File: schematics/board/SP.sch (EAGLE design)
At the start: 33 parts

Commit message: Плата СБ
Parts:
- added S1: (no value), CanCubeSat:255SB
- added U$1, U$2, U$20, U$21: KCONNECT--, CanCubeSat:KCONNECT--
- added U$18, U$3, U$4: KCONNECT4, CanCubeSat:KCONNECT4
- added U$19: KCONNECT1, CanCubeSat:KCONNECT1
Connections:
- removed net N$17: D24.C
- removed net N$18: D25.A
- removed net N$20: D26.A
- removed net N$23: D27.C
- removed net N$24: D28.A
- removed net N$26: D29.A
- removed net N$27: D29.C
- removed net N$29: SOL1.IN
- removed net N$30: D1.C, SOL16.OUT
- removed net N$31: D31.C
- removed net N$32: D32.A
- removed net N$33: D32.C
- removed net N$34: D33.A
- removed net N$35: D33.C
- removed net N$36: D34.A
- removed net N$37: D34.C
- removed net N$38: D35.A
- removed net N$39: D35.C
- removed net N$40: D36.A
- removed net N$41: D36.C
- removed net N$42: D37.A
- removed net N$43: D37.C
- removed net N$44: D38.A
- removed net N$45: D1.A, D38.C
- new net BUS+1: D1.A, D1.C, D38.C, U$1.P$1, U$18.P$1, U$20.P$1, U$3.P$1
- new net BUS-1: D29.A, S1.S, SOL1.IN
- new net N$2: S1.P, U$19.P$1, U$2.P$1, U$21.P$1, U$4.P$1
- net N$1: now also D29.C; no longer SOL1.OUT
- net N$10: now also D32.C, D33.A; no longer SOL10.OUT
- net N$11: now also D33.C, D34.A; no longer SOL11.OUT
- net N$12: now also D34.C, D35.A; no longer SOL12.OUT
- net N$13: now also D35.C, D36.A; no longer SOL13.OUT
- net N$14: now also D36.C, D37.A; no longer SOL14.OUT
- net N$15: now also D37.C, D38.A; no longer SOL15.OUT
- net N$16: no longer SOL2.OUT
- net N$19: now also D26.A; no longer SOL4.OUT
- net N$22: no longer SOL5.OUT
- net N$28: no longer SOL7.OUT
- net N$3: now also D24.C, D25.A; no longer SOL3.OUT
- net N$6: now also D27.C, D28.A; no longer SOL6.OUT
- net N$8: no longer SOL8.OUT
- net N$9: now also D31.C, D32.A; no longer SOL9.OUT

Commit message: Плата СБ
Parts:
- added LED1: LAP4-BOTTOM, led:LAP4-BOTTOM
- added R1: 2k7, rcl:R-US_R0603
- SOL1, SOL10, SOL11, SOL13, SOL14, SOL15, SOL2, SOL3, SOL5, SOL6, SOL7, SOL9: value SOLAR -> SOLAR_0; device CanCubeSat:SOLAR -> CanCubeSat:SOLAR_0
- SOL12, SOL16, SOL4, SOL8: value SOLARSOLAR_1 -> SOLAR_1; device CanCubeSat:SOLARSOLAR_1 -> CanCubeSat:SOLAR_1
- U$1, U$2, U$20, U$21: value KCONNECT-- -> KCONNECT3; device CanCubeSat:KCONNECT-- -> CanCubeSat:KCONNECT3
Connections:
- new net N$4: D1.A, D38.C, SOL16.OUT
- new net N$5: LED1.A, R1.1
- net BUS+1: now also R1.2; no longer D1.A, D38.C
- net N$1: now also SOL1.OUT
- net N$10: now also SOL10.OUT
- net N$11: now also SOL11.OUT
- net N$12: now also SOL12.OUT
- net N$13: now also SOL13.OUT
- net N$14: now also SOL14.OUT
- net N$15: now also SOL15.OUT
- net N$16: now also SOL2.OUT
- net N$19: now also SOL4.OUT
- net N$2: now also LED1.C
- net N$22: now also SOL5.OUT
- net N$28: now also SOL7.OUT
- net N$3: now also SOL3.OUT
- net N$6: now also SOL6.OUT
- net N$8: now also SOL8.OUT
- net N$9: now also SOL9.OUT

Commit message: Плата SP
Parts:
- removed LED1: LAP4-BOTTOM, led:LAP4-BOTTOM
- added PWR: (no value), led:LEDCHIPLED_0603
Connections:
- new net N$7: PWR.C
- net N$2: no longer LED1.C
- net N$5: now also PWR.A; no longer LED1.A
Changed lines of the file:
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@@
 <part name="U$21" library="CanCubeSat" deviceset="KCONNECT" device="3" value="KCONNECT3"/>
 <part name="S1" library="CanCubeSat" deviceset="255SB" device="" package3d_urn="urn:adsk.eagle:package:27679/1"/>
-<part name="LED1" library="led" library_urn="urn:adsk.eagle:library:259" deviceset="*P4" device="-BOTTOM" package3d_urn="urn:adsk.eagle:package:15878/1" technology="LA"/>
 <part name="R1" library="rcl" library_urn="urn:adsk.eagle:library:334" deviceset="R-US_" device="R0603" package3d_urn="urn:adsk.eagle:package:23555/3" value="2k7"/>
+<part name="PWR" library="led" library_urn="urn:adsk.eagle:library:259" deviceset="LED" device="CHIPLED_0603" package3d_urn="urn:adsk.eagle:package:15822/2"/>
 </parts>
 <sheets>
@@
 <attribute name="VALUE" x="36.83" y="-20.955" size="1.778" layer="96" rot="R270"/>
 </instance>
-<instance part="LED1" gate="G$1" x="66.04" y="7.62" smashed="yes">
-<attribute name="NAME" x="69.596" y="3.048" size="1.778" layer="95" rot="R90"/>
-<attribute name="VALUE" x="71.755" y="3.048" size="1.778" layer="96" rot="R90"/>
-</instance>
 <instance part="R1" gate="G$1" x="66.04" y="17.78" smashed="yes" rot="R90">
 <attribute name="NAME" x="64.5414" y="13.97" size="1.778" layer="95" rot="R90"/>
 <attribute name="VALUE" x="69.342" y="13.97" size="1.778" layer="96" rot="R90"/>
+</instance>
+<instance part="PWR" gate="G$1" x="66.04" y="7.62" smashed="yes">
+<attribute name="NAME" x="69.596" y="3.048" size="1.778" layer="95" rot="R90"/>
+<attribute name="VALUE" x="71.755" y="3.048" size="1.778" layer="96" rot="R90"/>
 </instance>
 </instances>
@@
 <label x="27.94" y="-5.08" size="1.778" layer="95" rot="R90"/>
 <label x="48.26" y="-5.08" size="1.778" layer="95" rot="R90"/>
-<pinref part="LED1" gate="G$1" pin="C"/>
 </segment>
 </net>
 <net name="N$5" class="0">
 <segment>
-<pinref part="LED1" gate="G$1" pin="A"/>
 <wire x1="66.04" y1="12.7" x2="66.04" y2="10.16" width="0.1524" layer="91"/>
 <pinref part="R1" gate="G$1" pin="1"/>
-</segment>
-</net>
+<pinref part="PWR" gate="G$1" pin="A"/>
+<junction x="66.04" y="10.16"/>
+</segment>
+</net>
+<net name="N$7" class="0">
+<segment>
+<pinref part="PWR" gate="G$1" pin="C"/>
+<junction x="66.04" y="2.54"/>
+</segment>
+</net>

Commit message: Плата SP
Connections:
- removed net BUS-1: D29.A, S1.S, SOL1.IN
- removed net N$7: PWR.C
- net N$2: now also D29.A, PWR.C, S1.S, SOL1.IN
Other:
- moved on the sheet: PWR
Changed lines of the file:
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@@
 <attribute name="VALUE" x="69.342" y="13.97" size="1.778" layer="96" rot="R90"/>
 </instance>
-<instance part="PWR" gate="G$1" x="66.04" y="7.62" smashed="yes">
-<attribute name="NAME" x="69.596" y="3.048" size="1.778" layer="95" rot="R90"/>
-<attribute name="VALUE" x="71.755" y="3.048" size="1.778" layer="96" rot="R90"/>
+<instance part="PWR" gate="G$1" x="66.04" y="5.08" smashed="yes">
+<attribute name="NAME" x="69.596" y="0.508" size="1.778" layer="95" rot="R90"/>
+<attribute name="VALUE" x="71.755" y="0.508" size="1.778" layer="96" rot="R90"/>
 </instance>
 </instances>
@@
 <wire x1="58.42" y1="25.4" x2="66.04" y2="25.4" width="0.1524" layer="91"/>
 <junction x="58.42" y="25.4"/>
-<wire x1="66.04" y1="25.4" x2="66.04" y2="22.86" width="0.1524" layer="91"/>
 <pinref part="R1" gate="G$1" pin="2"/>
-</segment>
-</net>
-<net name="BUS-1" class="0">
-<segment>
-<wire x1="-20.32" y1="-25.4" x2="-20.32" y2="-10.16" width="0.1524" layer="91"/>
-<wire x1="-20.32" y1="-10.16" x2="-17.78" y2="-10.16" width="0.1524" layer="91"/>
-<pinref part="D29" gate="G$1" pin="A"/>
-<wire x1="-17.78" y1="-25.4" x2="-20.32" y2="-25.4" width="0.1524" layer="91"/>
-<pinref part="SOL1" gate="G$1" pin="IN"/>
-<junction x="-20.32" y="-25.4"/>
-<wire x1="-20.32" y1="-25.4" x2="-25.4" y2="-25.4" width="0.1524" layer="91"/>
-<wire x1="27.94" y1="-22.86" x2="27.94" y2="-27.94" width="0.1524" layer="91"/>
-<wire x1="27.94" y1="-27.94" x2="-25.4" y2="-27.94" width="0.1524" layer="91"/>
-<wire x1="-25.4" y1="-27.94" x2="-25.4" y2="-25.4" width="0.1524" layer="91"/>
-<pinref part="S1" gate="1" pin="S"/>
+<wire x1="66.04" y1="22.86" x2="66.04" y2="25.4" width="0.1524" layer="91"/>
 </segment>
 </net>
@@
 <pinref part="U$21" gate="G$1" pin="P$1"/>
 <wire x1="58.42" y1="5.08" x2="58.42" y2="-5.08" width="0.1524" layer="91"/>
-<wire x1="66.04" y1="2.54" x2="66.04" y2="-5.08" width="0.1524" layer="91"/>
+<wire x1="66.04" y1="0" x2="66.04" y2="-5.08" width="0.1524" layer="91"/>
 <wire x1="66.04" y1="-5.08" x2="58.42" y2="-5.08" width="0.1524" layer="91"/>
 <junction x="58.42" y="-5.08"/>
@@
 <label x="27.94" y="-5.08" size="1.778" layer="95" rot="R90"/>
 <label x="48.26" y="-5.08" size="1.778" layer="95" rot="R90"/>
+<pinref part="PWR" gate="G$1" pin="C"/>
+</segment>
+<segment>
+<wire x1="-20.32" y1="-25.4" x2="-20.32" y2="-10.16" width="0.1524" layer="91"/>
+<wire x1="-20.32" y1="-10.16" x2="-17.78" y2="-10.16" width="0.1524" layer="91"/>
+<pinref part="D29" gate="G$1" pin="A"/>
+<wire x1="-17.78" y1="-25.4" x2="-20.32" y2="-25.4" width="0.1524" layer="91"/>
+<pinref part="SOL1" gate="G$1" pin="IN"/>
+<junction x="-20.32" y="-25.4"/>
+<wire x1="-20.32" y1="-25.4" x2="-25.4" y2="-25.4" width="0.1524" layer="91"/>
+<wire x1="27.94" y1="-22.86" x2="27.94" y2="-27.94" width="0.1524" layer="91"/>
+<wire x1="27.94" y1="-27.94" x2="-25.4" y2="-27.94" width="0.1524" layer="91"/>
+<wire x1="-25.4" y1="-27.94" x2="-25.4" y2="-25.4" width="0.1524" layer="91"/>
+<pinref part="S1" gate="1" pin="S"/>
+<label x="30.48" y="-27.94" size="1.778" layer="95"/>
 </segment>
 </net>
 <net name="N$5" class="0">
 <segment>
-<wire x1="66.04" y1="12.7" x2="66.04" y2="10.16" width="0.1524" layer="91"/>
+<wire x1="66.04" y1="12.7" x2="66.04" y2="7.62" width="0.1524" layer="91"/>
 <pinref part="R1" gate="G$1" pin="1"/>
 <pinref part="PWR" gate="G$1" pin="A"/>
-<junction x="66.04" y="10.16"/>
-</segment>
-</net>
-<net name="N$7" class="0">
-<segment>
-<pinref part="PWR" gate="G$1" pin="C"/>
-<junction x="66.04" y="2.54"/>
-</segment>
-</net>
+<junction x="66.04" y="7.62"/>
+</segment>
+</net>

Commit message: Плата SPv2
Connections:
- new net BUS-1: D29.A, S1.S, SOL1.IN
- net N$2: no longer D29.A, S1.S, SOL1.IN
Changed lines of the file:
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@@
 <label x="48.26" y="-5.08" size="1.778" layer="95" rot="R90"/>
 <pinref part="PWR" gate="G$1" pin="C"/>
+<label x="40.64" y="-5.08" size="1.778" layer="95"/>
 </segment>
+</net>
+<net name="N$5" class="0">
+<segment>
+<wire x1="66.04" y1="12.7" x2="66.04" y2="7.62" width="0.1524" layer="91"/>
+<pinref part="R1" gate="G$1" pin="1"/>
+<pinref part="PWR" gate="G$1" pin="A"/>
+<junction x="66.04" y="7.62"/>
+</segment>
+</net>
+<net name="BUS-1" class="0">
 <segment>
 <wire x1="-20.32" y1="-25.4" x2="-20.32" y2="-10.16" width="0.1524" layer="91"/>
@@
 </segment>
 </net>
-<net name="N$5" class="0">
-<segment>
-<wire x1="66.04" y1="12.7" x2="66.04" y2="7.62" width="0.1524" layer="91"/>
-<pinref part="R1" gate="G$1" pin="1"/>
-<pinref part="PWR" gate="G$1" pin="A"/>
-<junction x="66.04" y="7.62"/>
-</segment>
-</net>

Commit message: Плата SP с колодками
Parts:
- added JP1: (no value), pinhead:PINHD-1X2
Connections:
- net BUS+1: now also JP1.1
- net N$2: now also JP1.2
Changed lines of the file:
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@@
 <part name="R1" library="rcl" library_urn="urn:adsk.eagle:library:334" deviceset="R-US_" device="R0603" package3d_urn="urn:adsk.eagle:package:23555/3" value="2k7"/>
 <part name="PWR" library="led" library_urn="urn:adsk.eagle:library:259" deviceset="LED" device="CHIPLED_0603" package3d_urn="urn:adsk.eagle:package:15822/2"/>
+<part name="JP1" library="pinhead" library_urn="urn:adsk.eagle:library:325" deviceset="PINHD-1X2" device="" package3d_urn="urn:adsk.eagle:package:22435/2"/>
 </parts>
 <sheets>
@@
 <attribute name="NAME" x="69.596" y="0.508" size="1.778" layer="95" rot="R90"/>
 <attribute name="VALUE" x="71.755" y="0.508" size="1.778" layer="96" rot="R90"/>
+</instance>
+<instance part="JP1" gate="G$1" x="81.28" y="10.16" smashed="yes">
+<attribute name="NAME" x="74.93" y="15.875" size="1.778" layer="95"/>
+<attribute name="VALUE" x="74.93" y="5.08" size="1.778" layer="96"/>
 </instance>
 </instances>
@@
 <pinref part="R1" gate="G$1" pin="2"/>
 <wire x1="66.04" y1="22.86" x2="66.04" y2="25.4" width="0.1524" layer="91"/>
+<wire x1="66.04" y1="25.4" x2="73.66" y2="25.4" width="0.1524" layer="91"/>
+<junction x="66.04" y="25.4"/>
+<wire x1="73.66" y1="25.4" x2="73.66" y2="12.7" width="0.1524" layer="91"/>
+<pinref part="JP1" gate="G$1" pin="1"/>
+<wire x1="73.66" y1="12.7" x2="78.74" y2="12.7" width="0.1524" layer="91"/>
 </segment>
 </net>
@@
 <pinref part="PWR" gate="G$1" pin="C"/>
 <label x="40.64" y="-5.08" size="1.778" layer="95"/>
-</segment>
-</net>
+<wire x1="66.04" y1="-5.08" x2="73.66" y2="-5.08" width="0.1524" layer="91"/>
+<wire x1="73.66" y1="-5.08" x2="73.66" y2="10.16" width="0.1524" layer="91"/>
+<junction x="66.04" y="-5.08"/>
+<pinref part="JP1" gate="G$1" pin="2"/>
+<wire x1="73.66" y1="10.16" x2="78.74" y2="10.16" width="0.1524" layer="91"/>
+</segment>
+</net>

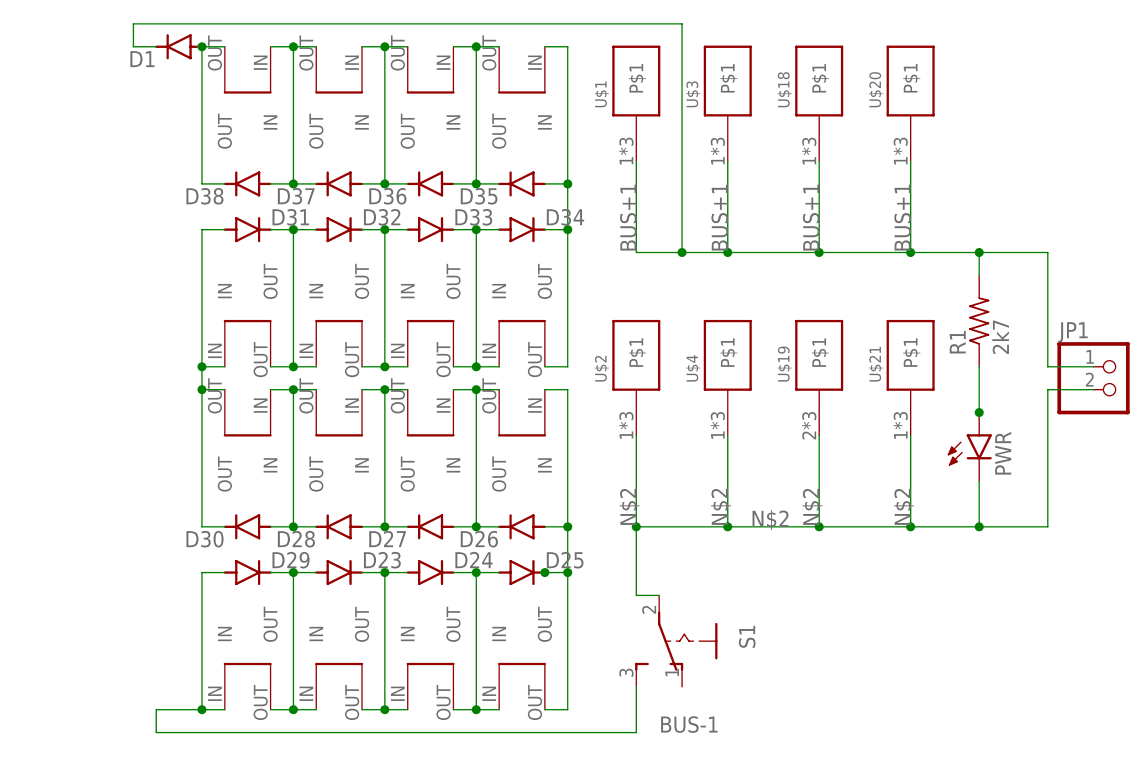
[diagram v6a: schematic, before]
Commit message: SP, убраны диоды, изменены площадки, добавлены надписи
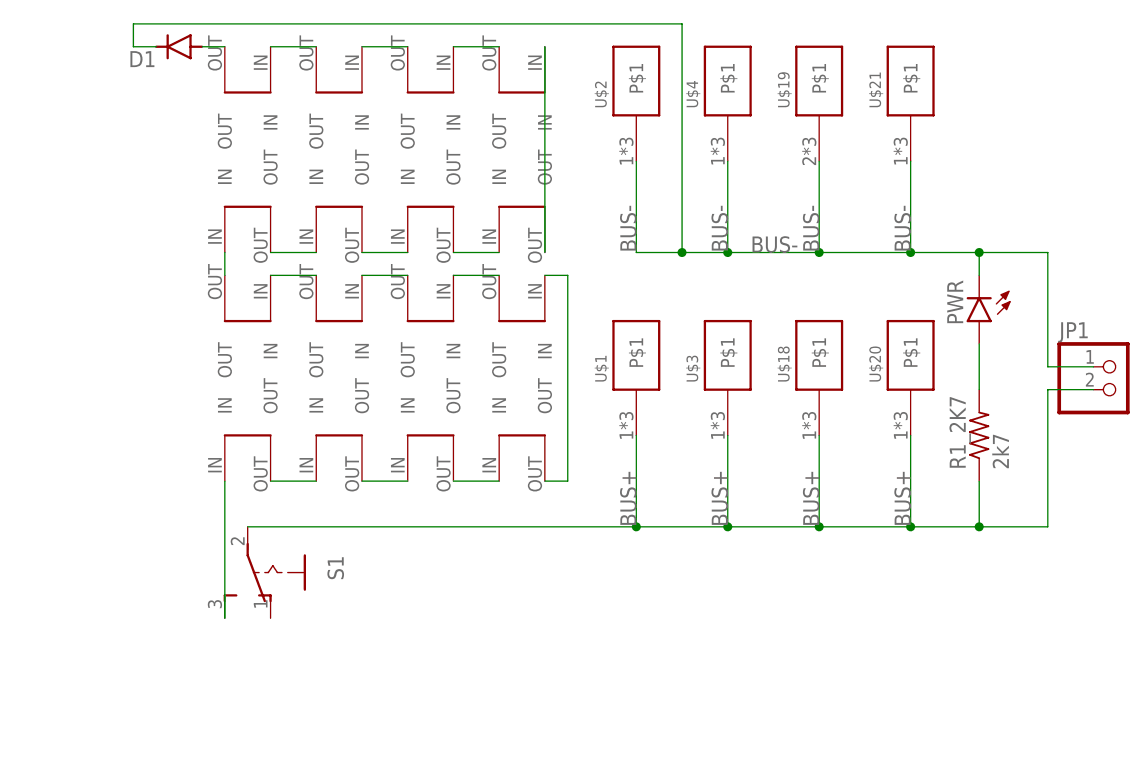
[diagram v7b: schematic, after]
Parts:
- removed D23, D24, D25, D26, D27, D28, D29, D30, D31, D32, D33, D34, D35, D36, D37, D38: MBR0520LT, diode:MBR0520LT
- removed R1: 2k7, rcl:R-US_R0603
- added R1_2K7: 2k7, rcl:R-US_R0603
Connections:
- removed net BUS+1: D1.C, JP1.1, R1.2, U$1.P$1, U$18.P$1, U$20.P$1, U$3.P$1
- removed net BUS-1: D29.A, S1.S, SOL1.IN
- removed net N$19: D25.C, D26.A, SOL4.OUT, SOL5.IN
- removed net N$2: JP1.2, PWR.C, S1.P, U$19.P$1, U$2.P$1, U$21.P$1, U$4.P$1
- removed net N$22: D26.C, D27.A, SOL5.OUT, SOL6.IN
- removed net N$28: D28.C, D30.A, SOL7.OUT, SOL8.IN
- new net BUS+: JP1.2, R1_2K7.1, S1.P, U$1.P$1, U$18.P$1, U$20.P$1, U$3.P$1
- new net BUS-: D1.C, JP1.1, PWR.C, U$19.P$1, U$2.P$1, U$21.P$1, U$4.P$1
- new net N$17: SOL14.OUT, SOL15.IN
- new net N$18: SOL15.OUT, SOL16.IN
- new net N$24: SOL4.OUT, SOL5.IN
- new net N$7: S1.S, SOL1.IN
- net N$1: no longer D23.A, D29.C
- net N$10: now also SOL7.OUT, SOL8.IN; no longer D32.C, D33.A, SOL10.OUT, SOL11.IN
- net N$11: now also SOL8.OUT, SOL9.IN; no longer D33.C, D34.A, SOL11.OUT, SOL12.IN
- net N$12: now also SOL10.IN, SOL9.OUT; no longer D34.C, D35.A, SOL12.OUT, SOL13.IN
- net N$13: now also SOL10.OUT, SOL11.IN; no longer D35.C, D36.A, SOL13.OUT, SOL14.IN
- net N$14: now also SOL11.OUT, SOL12.IN; no longer D36.C, D37.A, SOL14.OUT, SOL15.IN
- net N$15: now also SOL12.OUT, SOL13.IN; no longer D37.C, D38.A, SOL15.OUT, SOL16.IN
- net N$16: now also SOL13.OUT, SOL14.IN; no longer D23.C, D24.A, SOL2.OUT, SOL3.IN
- net N$3: now also SOL2.OUT, SOL3.IN; no longer D24.C, D25.A, SOL3.OUT, SOL4.IN
- net N$4: no longer D38.C
- net N$5: now also R1_2K7.2; no longer R1.1
- net N$6: now also SOL3.OUT, SOL4.IN; no longer D27.C, D28.A, SOL6.OUT, SOL7.IN
- net N$8: now also SOL5.OUT, SOL6.IN; no longer D30.C, D31.A, SOL8.OUT, SOL9.IN
- net N$9: now also SOL6.OUT, SOL7.IN; no longer D31.C, D32.A, SOL10.IN, SOL9.OUT
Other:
- moved on the sheet: PWR, S1, U$1, U$18, U$19, U$2, U$20, U$21, U$3, U$4
